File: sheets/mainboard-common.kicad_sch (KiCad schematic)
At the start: 45 parts, among them J1 Conn_01x04, J2 USB4105, J3 Conn_01x04, J4 Conn_01x16_Socket, J5 Conn_01x16_Socket, J6 Conn_01x16_Socket, J7 Conn_01x16_Socket, U4 AP22916, U5 AP22916

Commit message: More cleanup
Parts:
- renumbered C5 to C1, C21 to C10, C23 to C11, C22 to C12, C25 to C2, C7 to C3, C14 to C4, C19 to C5, C13 to C6, C15 to C7, C16 to C8, C24 to C9, J3 to J1, J1 to J3, J6 to J5, J7 to J6, J5 to J7, LED2 to LED1, R21 to R1, R16 to R10, R24 to R11, R23 to R2, R4 to R3, R5 to R4, R10 to R5, R20 to R6, R13 to R7, R15 to R8, R19 to R9, TP3 to TP2, TP4 to TP3, TP5 to TP4, TP8 to TP5, U5 to U2, U4 to U3

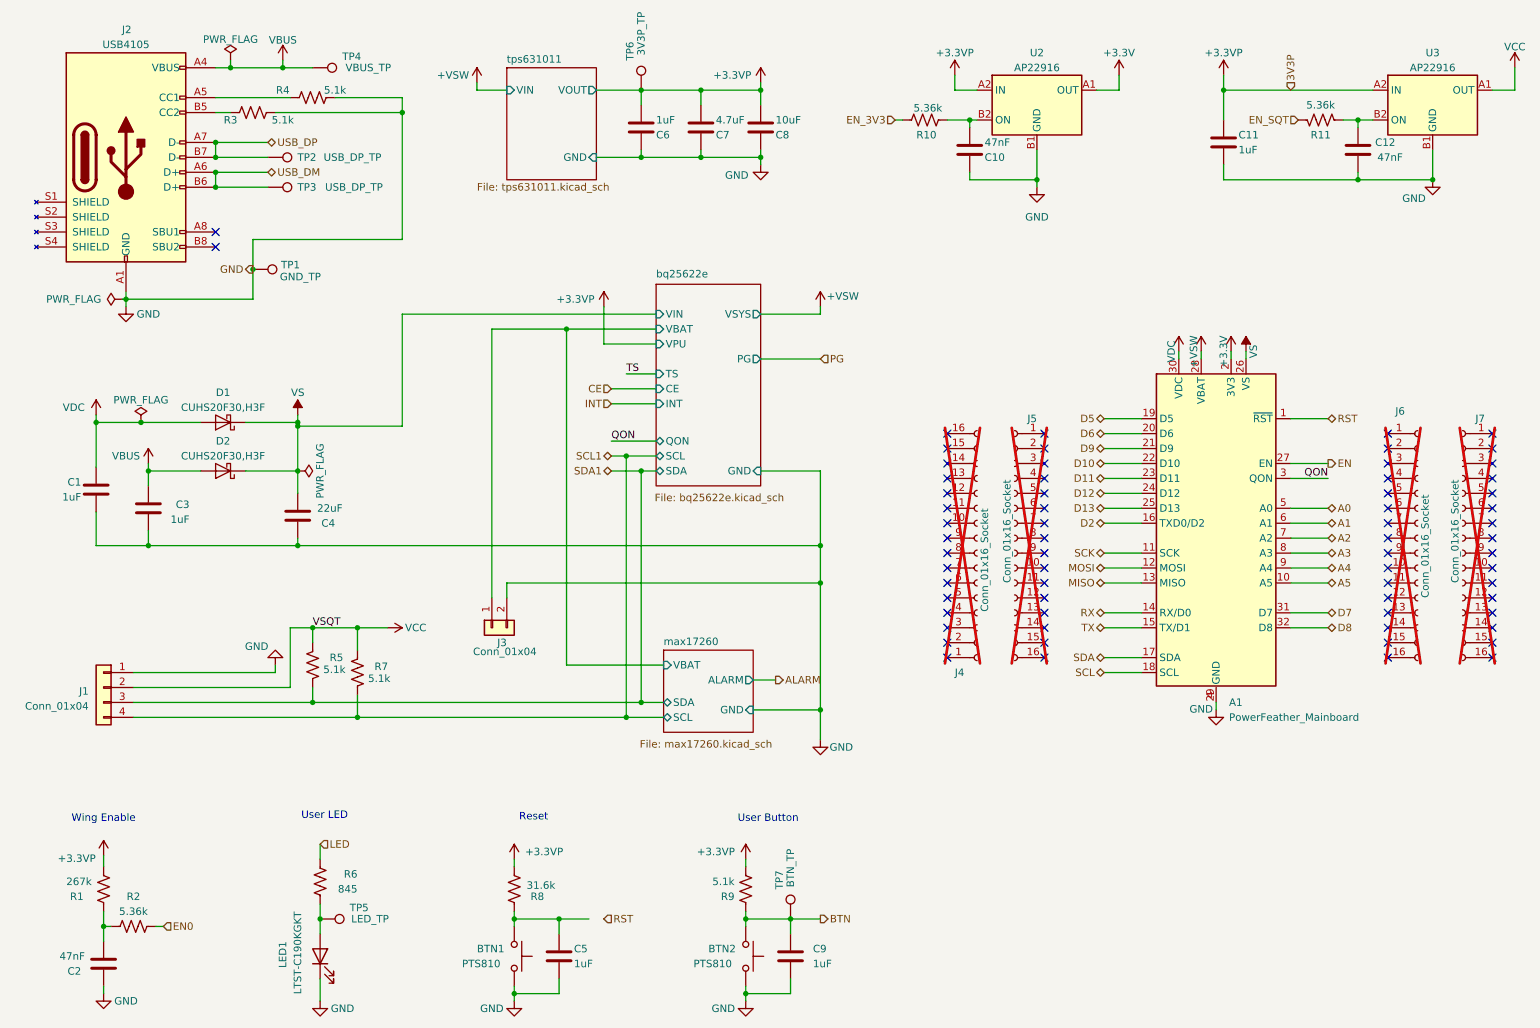
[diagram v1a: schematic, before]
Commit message: Fix max17260 schematic
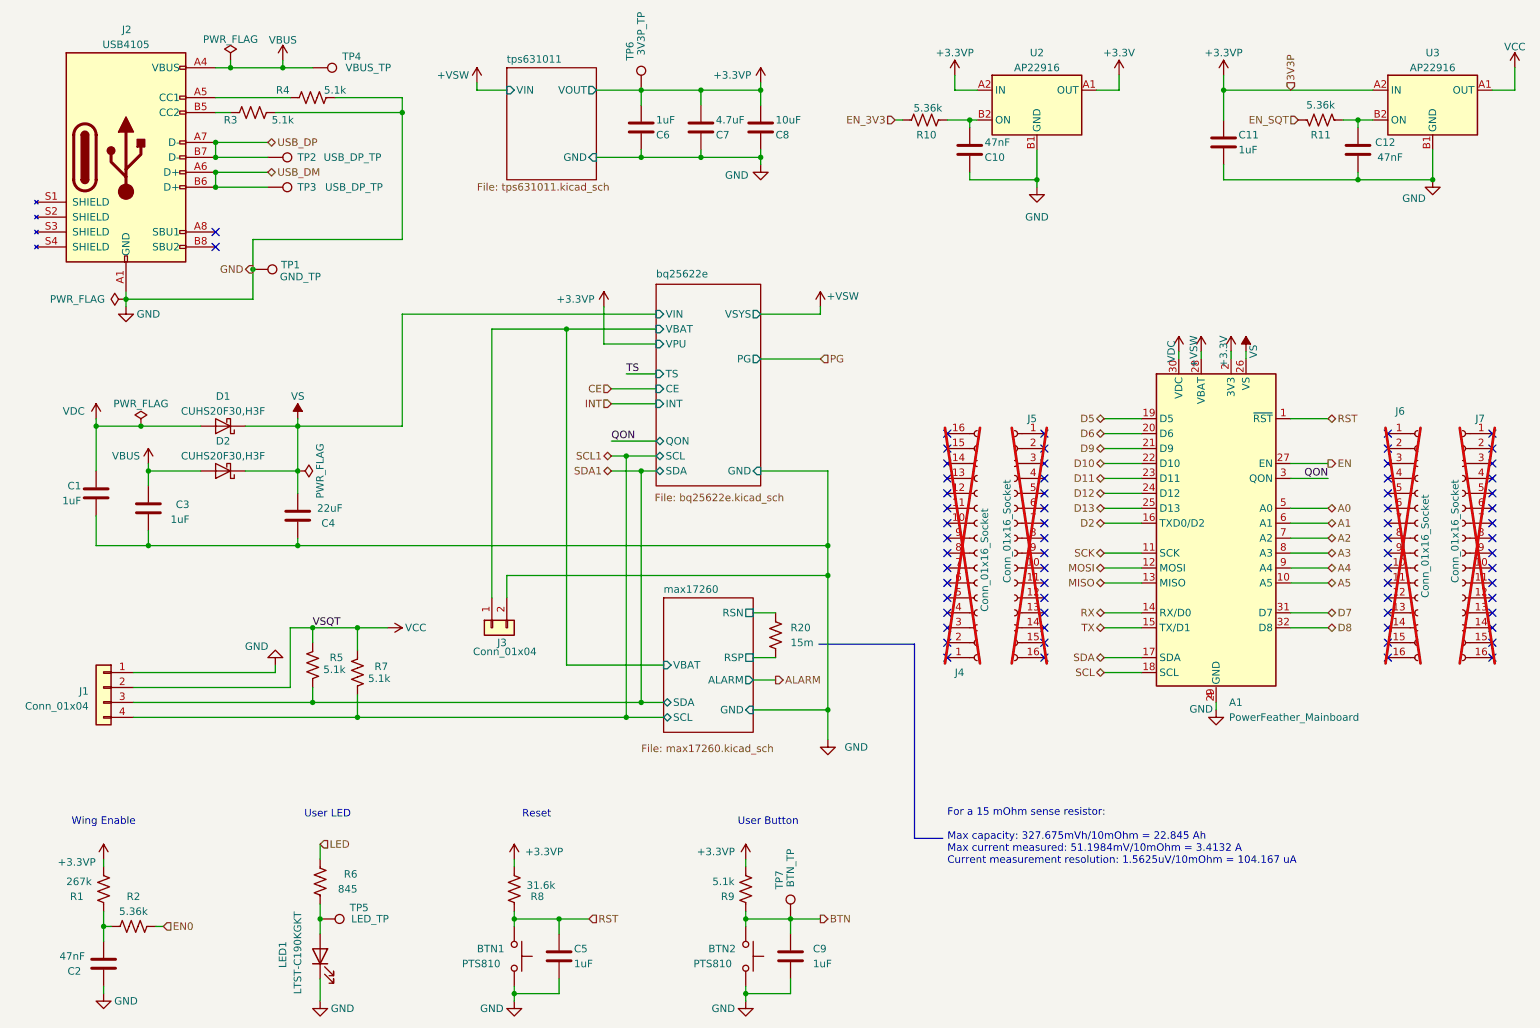
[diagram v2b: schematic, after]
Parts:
- added R20: 15m, Resistor_SMD:R_0603_1608Metric, symbol Device:R_US
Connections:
- net RST: now also BTN1.1, C5.2, R8.1
- new net max17260/RSN: R20.1
- new net max17260/RSP: R20.2
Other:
- sheet max17260 ports: added RSN, RSP; removed none
- note added: "For a 15 mOhm sense resistor: Max capacity: 327.675mVh/10mOhm = 22.845 Ah Max current measured: 51.1984mV/10mOhm = 3.4132 A Current measurement resolution: 1.5625uV/10mOhm = 104.167 uA"
- moved on the sheet: C1, D1
